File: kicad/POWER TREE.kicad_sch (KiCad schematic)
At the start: 0 parts

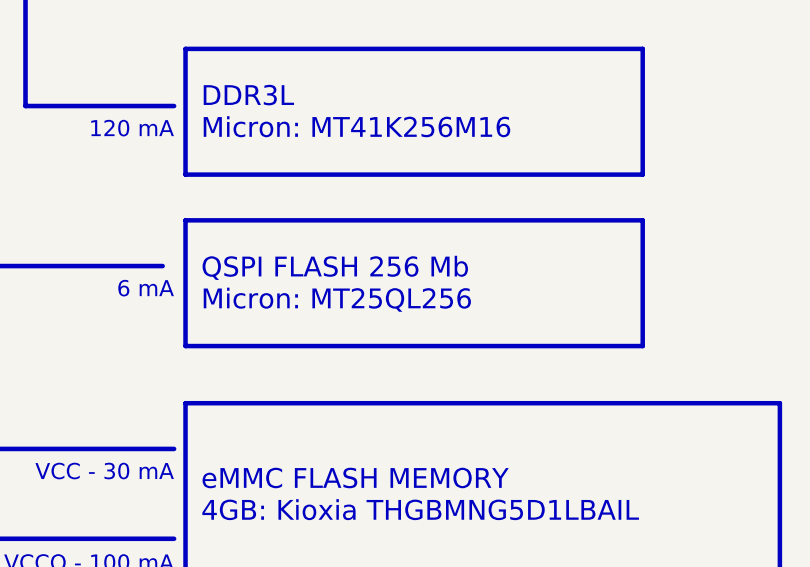
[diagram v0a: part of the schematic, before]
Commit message: Change schematic and PCB
  changed component U11 from 8MBit to 32 MBit
  added qr-code on bottom overlay
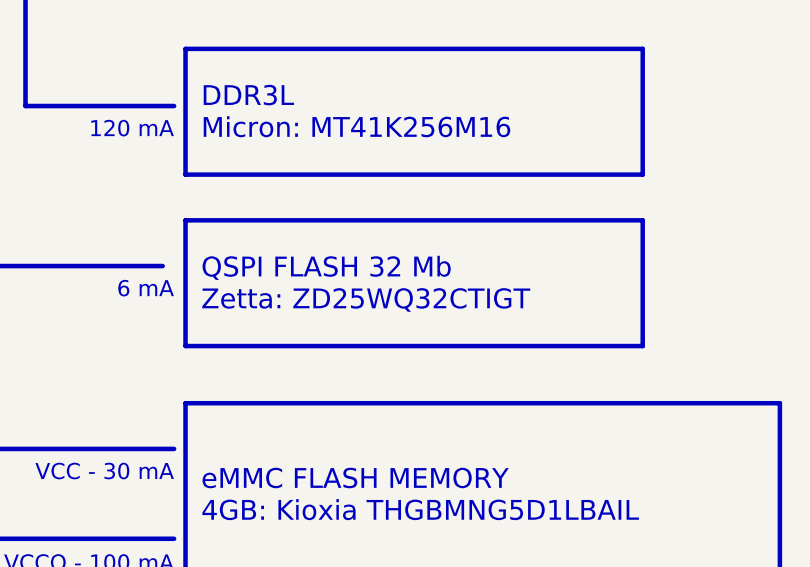
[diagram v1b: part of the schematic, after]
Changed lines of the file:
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@@
 		)
 	)
-	(text_box "QSPI FLASH 256 Mb\n    Micron: MT25QL256"
+	(text_box "QSPI FLASH 32 Mb\n    Zetta: ZD25WQ32CTIGT"
 		(exclude_from_sim no)
 		(at 254 200.66 0)

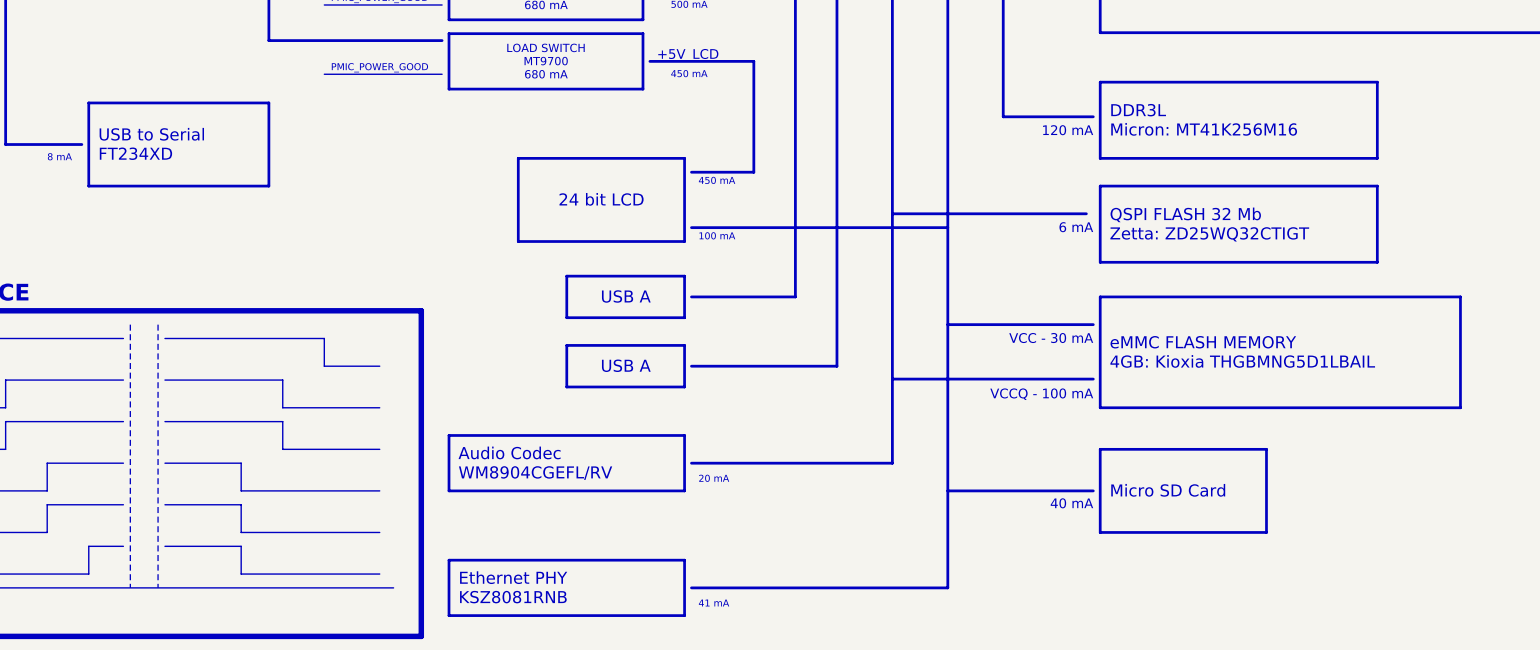
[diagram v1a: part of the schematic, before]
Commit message: Fix hardware bugs - Fix part number in bom for resistors R103, R113, R114, R118 -> 680K - Fix part number in BOM for resistors R13, R16 -> 68K - Fix part number in BOM for resistor R14 -> 4.7K - Fix part number in BOM for capacitors C100, C101, C12, C13, C130, C131, C133, C135, C140, C141, C15, C19, C57, C58, C7, C99 -> 100nF - Fix footprint for USB-A connectors - Fix power buttom pull-up resistor connection -> connect to +3.3V_STAND_BY
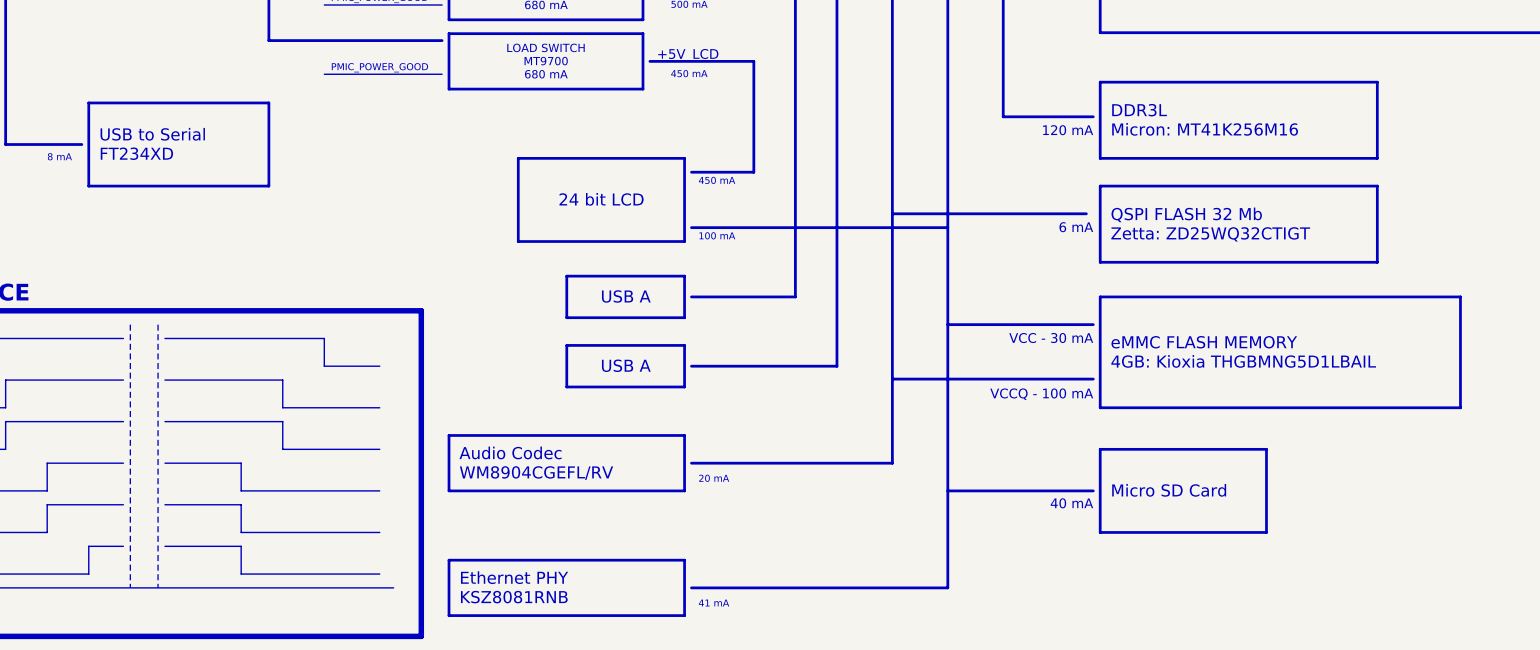
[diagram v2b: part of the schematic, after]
